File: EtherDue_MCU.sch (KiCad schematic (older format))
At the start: 30 parts, among them SW301 ERASE, SW302 RESET, U301 ATSAM3X8E, U302 FDN340P, U303 LMV358IDGKR, X301 12MHz KX-7 20pF, X302 32.768kHz

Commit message: Final ERC cleanup, export net file
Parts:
- renumbered C301 to C201, C302 to C202, C303 to C203, C304 to C204, C305 to C205, C306 to C206, C307 to C207, C308 to C208, D301 to D201, D302 to D202, D303 to D203, D304 to D204, JR301 to JR201, JR302 to JR202, JR303 to JR203, L301 to L201, R301 to R201, R302 to R202, R303 to R203, R304 to R204, R305 to R205, R306 to R206, SW301 to SW201, SW302 to SW202, U301 to U201, U302 to U202, U303 to U203, X301 to X201, X302 to X202
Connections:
- net +3.3V: now also R206.1 (7), R206.6 (8), R206.8; no longer R206.2 (8), R206.4 (8), R206.5 (7)
- net at D203.A: now also R206.2 (8); no longer R206.6 (8)
- net at U203.1, U203.2 (-): now also R206.3 (7); no longer R206.7
- net at D204.A: now also R206.4 (8); no longer R206.8
- net at D202.A: now also R206.7; no longer R206.3 (7)
- net at D201.A: now also R206.5 (7); no longer R206.1 (7)
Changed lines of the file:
@@
-EESchema Schematic File Version 2  date Thu 11 Apr 2013 15:52:58 EST
+EESchema Schematic File Version 2  date Thu 11 Apr 2013 16:32:55 EST
 LIBS:power
 LIBS:device
@@
 JTAG
 $Comp
-L ATSAM3X8E U301
+L ATSAM3X8E U201
 U 1 1 515B964D
 P 7900 5650
-F 0 "U301" H 5900 3050 50  0000 C CNN
+F 0 "U201" H 5900 3050 50  0000 C CNN
 F 1 "ATSAM3X8E" H 6050 2950 50  0000 C CNN
 F 2 "MODULE" H 6500 3550 50  0001 C CNN
@@
 $EndComp
 $Comp
-L RES_PACK4_IND R305
+L RES_PACK4_IND R205
 U 2 1 5163C001
 P 7300 10150
-F 0 "R305" H 7000 10200 50  0000 C CNN
+F 0 "R205" H 7000 10200 50  0000 C CNN
 F 1 "1K5" H 7300 10050 50  0000 C CNN
 F 2 "" H 7300 10150 60  0001 C CNN
@@
 $EndComp
 $Comp
-L RES_PACK4_IND R305
+L RES_PACK4_IND R205
 U 1 1 5163BFF9
 P 6900 10150
-F 0 "R305" H 6600 10200 50  0000 C CNN
+F 0 "R205" H 6600 10200 50  0000 C CNN
 F 1 "1K5" H 6900 10050 50  0000 C CNN
 F 2 "" H 6900 10150 60  0001 C CNN
@@
 $EndComp
 $Comp
-L R JR301
+L R JR201
 U 1 1 5163BF82
 P 5250 3200
-F 0 "JR301" V 5350 3200 50  0000 C CNN
+F 0 "JR201" V 5350 3200 50  0000 C CNN
 F 1 "0R / NOT PLACED" V 5150 3200 50  0000 C CNN
 F 2 "" H 5250 3200 60  0001 C CNN
@@
 $EndComp
 $Comp
-L R JR303
+L R JR203
 U 1 1 5163BF2B
 P 5800 1150
-F 0 "JR303" V 5880 1150 50  0000 C CNN
+F 0 "JR203" V 5880 1150 50  0000 C CNN
 F 1 "0R NOT PLACED" V 5700 1150 50  0000 C CNN
 F 2 "" H 5800 1150 60  0001 C CNN
@@
 VDDOUT
 $Comp
-L SW_PUSHBUTTON SW302
+L SW_PUSHBUTTON SW202
 U 1 1 515CF2B2
 P 13000 2550
-F 0 "SW302" H 12850 2660 50  0000 C CNN
+F 0 "SW202" H 12850 2660 50  0000 C CNN
 F 1 "RESET" H 13000 2470 50  0000 C CNN
 F 2 "" H 13000 2550 60  0001 C CNN
@@
 $EndComp
 $Comp
-L C C308
+L C C208
 U 1 1 515CF2B0
 P 13000 1950
-F 0 "C308" H 13050 2050 50  0000 L CNN
+F 0 "C208" H 13050 2050 50  0000 L CNN
 F 1 "10nF" H 13050 1850 50  0000 L CNN
 F 2 "" H 13000 1950 60  0001 C CNN
@@
 ERASE
 $Comp
-L MOSFET-PCHANNEL U302
+L MOSFET-PCHANNEL U202
 U 1 1 515CF01A
 P 12000 8950
-F 0 "U302" V 11700 8700 70  0000 L BNN
+F 0 "U202" V 11700 8700 70  0000 L BNN
 F 1 "FDN340P" V 11800 8400 70  0000 L BNN
 F 2 "" H 12000 8950 60  0001 C CNN
@@
 $EndComp
 $Comp
-L SW_PUSHBUTTON SW301
+L SW_PUSHBUTTON SW201
 U 1 1 515CF006
 P 12100 8400
-F 0 "SW301" H 11950 8510 50  0000 C CNN
+F 0 "SW201" H 11950 8510 50  0000 C CNN
 F 1 "ERASE" H 12100 8320 50  0000 C CNN
 F 2 "" H 12100 8400 60  0001 C CNN
@@
 PWM13
 $Comp
-L RES_PACK4_IND R306
-U 1 1 515CBE59
+L RES_PACK4_IND R206
+U 3 1 515CBE59
 P 14450 6500
-F 0 "R306" H 14150 6550 50  0000 C CNN
+F 0 "R206" H 14150 6550 50  0000 C CNN
 F 1 "1K" H 14450 6400 50  0000 C CNN
 F 2 "" H 14450 6500 60  0001 C CNN
 F 3 "" H 14450 6500 60  0001 C CNN
-	1    14450 6500
-	1    0    0    -1
-$EndComp
-$Comp
-L RES_PACK4_IND R306
-U 2 1 515CBE58
+	3    14450 6500
+	1    0    0    -1
+$EndComp
+$Comp
+L RES_PACK4_IND R206
+U 4 1 515CBE58
 P 14450 6800
-F 0 "R306" H 14150 6850 50  0000 C CNN
+F 0 "R206" H 14150 6850 50  0000 C CNN
 F 1 "1K" H 14450 6700 50  0000 C CNN
 F 2 "" H 14450 6800 60  0001 C CNN
 F 3 "" H 14450 6800 60  0001 C CNN
-	2    14450 6800
+	4    14450 6800
 	1    0    0    -1
 $EndComp
@@
 $EndComp
 $Comp
-L LED D301
+L LED D201
 U 1 1 515CBE56
 P 13800 6500
-F 0 "D301" H 13800 6600 50  0000 C CNN
+F 0 "D201" H 13800 6600 50  0000 C CNN
 F 1 "YELLOW" H 13800 6400 50  0000 C CNN
 F 2 "" H 13800 6500 60  0001 C CNN
@@
 $EndComp
 $Comp
-L LED D302
+L LED D202
 U 1 1 515CBE55
 P 13800 6800
-F 0 "D302" H 13800 6900 50  0000 C CNN
+F 0 "D202" H 13800 6900 50  0000 C CNN
 F 1 "YELLOW" H 13800 6700 50  0000 C CNN
 F 2 "" H 13800 6800 60  0001 C CNN
@@
 $EndComp
 $Comp
-L LED D304
+L LED D204
 U 1 1 515CBD0A
 P 14950 5500
-F 0 "D304" H 14950 5600 50  0000 C CNN
+F 0 "D204" H 14950 5600 50  0000 C CNN
 F 1 "YELLOW" H 14950 5400 50  0000 C CNN
 F 2 "" H 14950 5500 60  0001 C CNN
@@
 $EndComp
 $Comp
-L LED D303
+L LED D203
 U 1 1 515CBD09
 P 14950 5150
-F 0 "D303" H 14950 5250 50  0000 C CNN
+F 0 "D203" H 14950 5250 50  0000 C CNN
 F 1 "GREEN" H 14950 5050 50  0000 C CNN
 F 2 "" H 14950 5150 60  0001 C CNN
@@
 $EndComp
 $Comp
-L LM358 U303
+L LM358 U203
 U 1 1 515CBD06
 P 13250 5500
-F 0 "U303" H 13200 5700 60  0000 L CNN
+F 0 "U203" H 13200 5700 60  0000 L CNN
 F 1 "LMV358IDGKR" H 13200 5250 60  0000 L CNN
 F 2 "" H 13250 5500 60  0001 C CNN
@@
 $Comp
 L RES_PACK4_IND R206
-U 4 1 515CBD03
+U 2 1 515CBD03
 P 14150 5500
 F 0 "R206" H 13850 5550 50  0000 C CNN
@@
 F 2 "" H 14150 5500 60  0001 C CNN
 F 3 "" H 14150 5500 60  0001 C CNN
-	4    14150 5500
+	2    14150 5500
 	1    0    0    -1
 $EndComp
@@
 $Comp
 L RES_PACK4_IND R206
-U 3 1 515CBD02
+U 1 1 515CBD02
 P 14150 5150
 F 0 "R206" H 13850 5200 50  0000 C CNN
@@
 F 2 "" H 14150 5150 60  0001 C CNN
 F 3 "" H 14150 5150 60  0001 C CNN
-	3    14150 5150
+	1    14150 5150
 	1    0    0    -1
 $EndComp
@@
 $EndComp
 $Comp
-L R R301
+L R R201
 U 1 1 515BAA3A
 P 3400 5500
-F 0 "R301" V 3480 5500 50  0000 C CNN
+F 0 "R201" V 3480 5500 50  0000 C CNN
 F 1 "6k8 1%" V 3400 5500 50  0000 C CNN
 F 2 "" H 3400 5500 60  0001 C CNN
@@
 $EndComp
 $Comp
-L C C305
+L C C205
 U 1 1 515BAA2B
 P 3800 5500
-F 0 "C305" H 3850 5600 50  0000 L CNN
+F 0 "C205" H 3850 5600 50  0000 L CNN
 F 1 "22pF" H 3850 5400 50  0000 L CNN
 F 2 "" H 3800 5500 60  0001 C CNN
@@
 $EndComp
 $Comp
-L R R302
+L R R202
 U 1 1 515BA9DE
 P 5200 4100
-F 0 "R302" V 5280 4100 50  0000 C CNN
+F 0 "R202" V 5280 4100 50  0000 C CNN
 F 1 "39R 1%" V 5200 4100 50  0000 C CNN
 F 2 "" H 5200 4100 60  0001 C CNN
@@
 $EndComp
 $Comp
-L R R303
+L R R203
 U 1 1 515BA9D0
 P 5200 4300
-F 0 "R303" V 5280 4300 50  0000 C CNN
+F 0 "R203" V 5280 4300 50  0000 C CNN
 F 1 "39R 1%" V 5200 4300 50  0000 C CNN
 F 2 "" H 5200 4300 60  0001 C CNN
@@
 $EndComp
 $Comp
-L C C304
+L C C204
 U 1 1 515BA7F4
 P 3200 4900
-F 0 "C304" H 3250 5000 50  0000 L CNN
+F 0 "C204" H 3250 5000 50  0000 L CNN
 F 1 "22pF_NM" V 3300 4500 50  0000 L CNN
 F 2 "" H 3200 4900 60  0001 C CNN
@@
 $EndComp
 $Comp
-L C C303
+L C C203
 U 1 1 515BA7D3
 P 3200 4150
-F 0 "C303" H 3250 4250 50  0000 L CNN
+F 0 "C203" H 3250 4250 50  0000 L CNN
 F 1 "22pF_NM" V 3300 3750 50  0000 L CNN
 F 2 "" H 3200 4150 60  0001 C CNN
@@
 $EndComp
 $Comp
-L CRYSTAL X302
+L CRYSTAL X202
 U 1 1 515BA7AB
 P 3750 4450
-F 0 "X302" H 3750 4600 60  0000 C CNN
+F 0 "X202" H 3750 4600 60  0000 C CNN
 F 1 "32.768kHz" H 3750 4300 60  0000 C CNN
 F 2 "" H 3750 4450 60  0001 C CNN
@@
 $EndComp
 $Comp
-L C C302
+L C C202
 U 1 1 515BA78E
 P 3200 3750
-F 0 "C302" H 3250 3850 50  0000 L CNN
+F 0 "C202" H 3250 3850 50  0000 L CNN
 F 1 "22pF" H 3250 3650 50  0000 L CNN
 F 2 "" H 3200 3750 60  0001 C CNN
@@
 $EndComp
 $Comp
-L C C301
+L C C201
 U 1 1 515BA78B
 P 3200 2700
-F 0 "C301" H 3250 2800 50  0000 L CNN
+F 0 "C201" H 3250 2800 50  0000 L CNN
 F 1 "22pF" H 3250 2600 50  0000 L CNN
 F 2 "" H 3200 2700 60  0001 C CNN
@@
 $EndComp
 $Comp
-L CRYSTAL X301
+L CRYSTAL X201
 U 1 1 515BA76A
 P 3750 3150
-F 0 "X301" H 3750 3300 60  0000 C CNN
+F 0 "X201" H 3750 3300 60  0000 C CNN
 F 1 "12MHz KX-7 20pF" H 3800 3000 60  0000 C CNN
 F 2 "" H 3750 3150 60  0001 C CNN
@@
 $EndComp
 $Comp
-L R JR302
+L R JR202
 U 1 1 515BA19D
 P 5800 950
-F 0 "JR302" V 5880 950 50  0000 C CNN
+F 0 "JR202" V 5880 950 50  0000 C CNN
 F 1 "0R" V 5800 950 50  0000 C CNN
 F 2 "" H 5800 950 60  0001 C CNN
@@
 $EndComp
 $Comp
-L C C306
+L C C206
 U 1 1 515B9982
 P 6300 1450
-F 0 "C306" H 6350 1550 50  0000 L CNN
+F 0 "C206" H 6350 1550 50  0000 L CNN
 F 1 "100nF" H 6350 1350 50  0000 L CNN
 F 2 "" H 6300 1450 60  0001 C CNN
@@
 $EndComp
 $Comp
-L C C307
+L C C207
 U 1 1 515B9979
 P 7150 1350
-F 0 "C307" H 7050 1450 50  0000 L CNN
+F 0 "C207" H 7050 1450 50  0000 L CNN
 F 1 "100nF" H 6900 1250 50  0000 L CNN
 F 2 "" H 7150 1350 60  0001 C CNN
@@
 $EndComp
 $Comp
-L INDUCTOR L301
+L INDUCTOR L201
 U 1 1 515B996F
 P 6700 1100
-F 0 "L301" V 6650 1100 40  0000 C CNN
+F 0 "L201" V 6650 1100 40  0000 C CNN
 F 1 "MH2029-300Y" V 6800 1100 40  0000 C CNN
 F 2 "" H 6700 1100 60  0001 C CNN
@@
 $EndComp
 $Comp
-L R R304
+L R R204
 U 1 1 515B98E9
 P 6750 2300
-F 0 "R304" V 6830 2300 50  0000 C CNN
+F 0 "R204" V 6830 2300 50  0000 C CNN
 F 1 "100K" V 6750 2300 50  0000 C CNN
 F 2 "" H 6750 2300 60  0001 C CNN

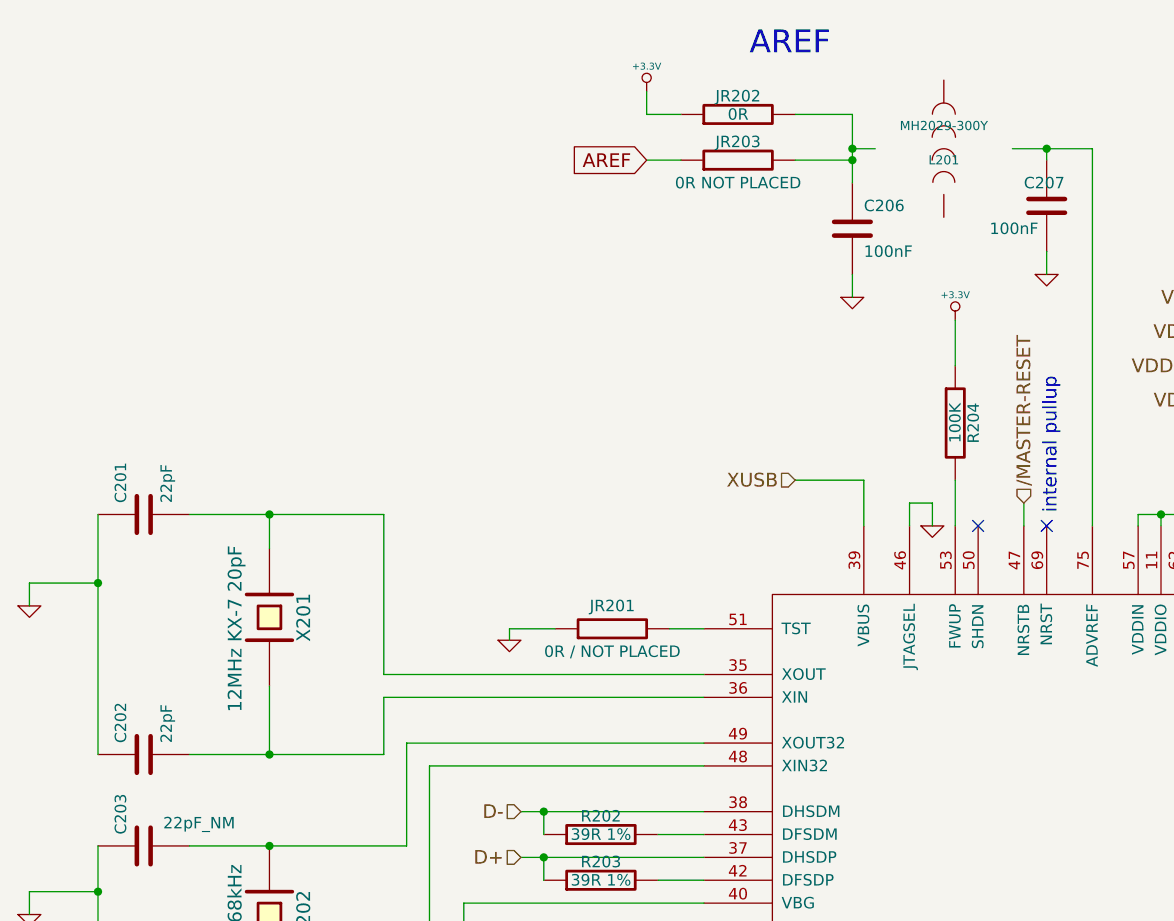
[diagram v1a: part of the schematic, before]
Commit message: Edit pass of footprints, cleanup symbols, etc.
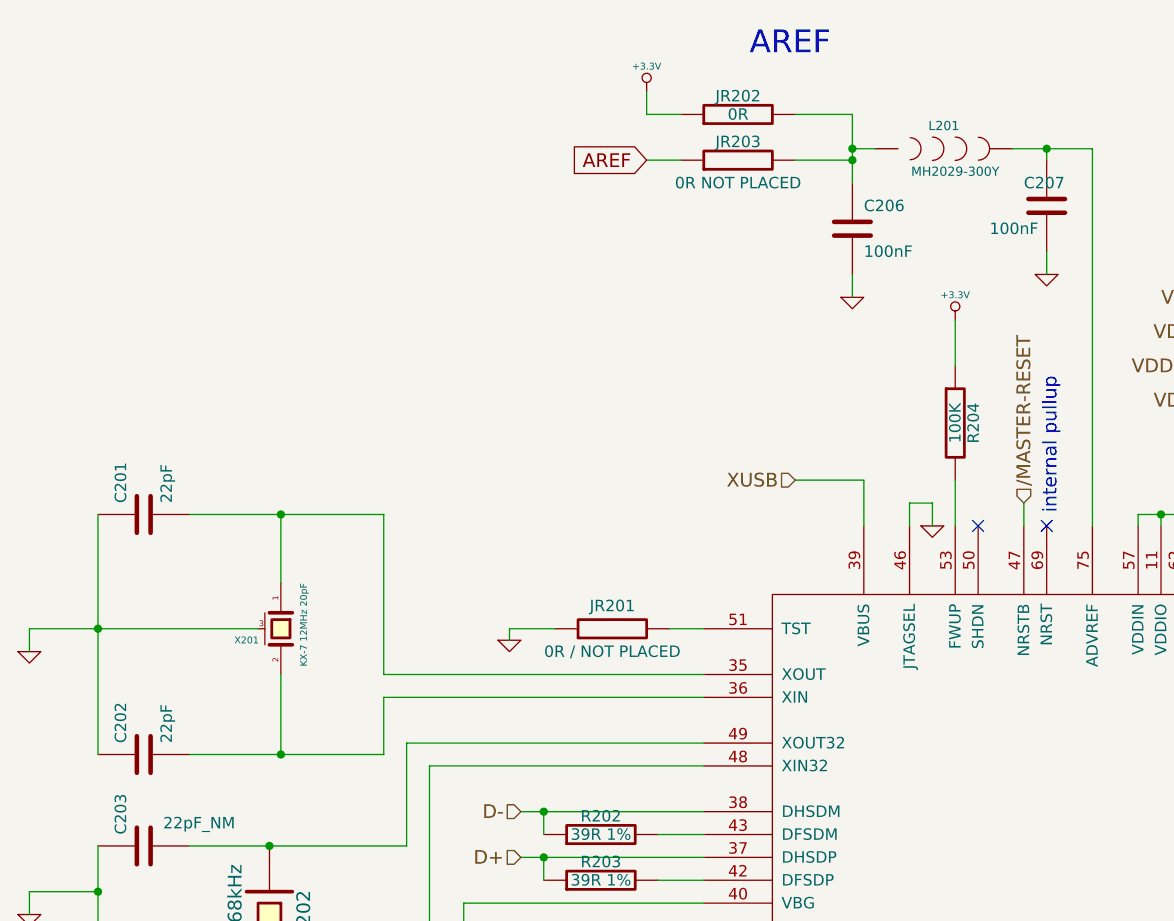
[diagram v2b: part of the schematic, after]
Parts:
- removed X201: 12MHz KX-7 20pF, symbol CRYSTAL
- added X201: KX-7 12MHz 20pF, ~, symbol CRYSTAL_SMD
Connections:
- net GND: now also X201.3 (case)
- net at C201.2, U201.35 (XOUT): now also X201.1
- net at C202.2, U201.36 (XIN): now also X201.2
- net at C207.1, U201.75 (ADVREF): now also L201.2
- net at L201.1: now also C206.1, JR202.2, JR203.2
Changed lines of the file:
@@
-EESchema Schematic File Version 2  date Thu 11 Apr 2013 16:32:55 EST
+EESchema Schematic File Version 2  date Fri 03 May 2013 15:34:29 EST
+LIBS:freetronics_kicad_sch_lib
 LIBS:power
 LIBS:device
@@
 LIBS:contrib
 LIBS:valves
-LIBS:freetronics_kicad_sch_lib
 LIBS:EtherDue-cache
 EELAYER 24 0
@@
 Sheet 2 6
 Title ""
-Date "11 apr 2013"
+Date "3 may 2013"
 Rev ""
 Comp ""
@@
 Wire Wire Line
 	2700 4350 2700 4450
-Connection ~ 3750 3750
 Wire Wire Line
 	5650 3500 4250 3500
@@
 Wire Wire Line
 	4250 3750 3400 3750
-Connection ~ 3000 3000
+Connection ~ 3000 3200
 Wire Wire Line
 	3000 3750 3000 2700
-Connection ~ 3750 2700
 Wire Wire Line
 	3400 2700 4250 2700
@@
 Wire Wire Line
 	4250 3400 5650 3400
-Wire Wire Line
-	3750 2700 3750 2850
-Wire Wire Line
-	3000 3000 2700 3000
-Wire Wire Line
-	2700 3000 2700 3100
-Wire Wire Line
-	3750 3750 3750 3450
 Wire Wire Line
 	3000 4150 3000 4900
@@
 L GND #PWR010
 U 1 1 515BA7A2
-P 2700 3100
-F 0 "#PWR010" H 2700 3100 30  0001 C CNN
-F 1 "GND" H 2700 3030 30  0001 C CNN
-F 2 "" H 2700 3100 60  0001 C CNN
-F 3 "" H 2700 3100 60  0001 C CNN
-	1    2700 3100
+P 2700 3300
+F 0 "#PWR010" H 2700 3300 30  0001 C CNN
+F 1 "GND" H 2700 3230 30  0001 C CNN
+F 2 "" H 2700 3300 60  0001 C CNN
+F 3 "" H 2700 3300 60  0001 C CNN
+	1    2700 3300
 	1    0    0    -1
 $EndComp
@@
 	1    3200 2700
 	0    -1   -1   0
-$EndComp
-$Comp
-L CRYSTAL X201
-U 1 1 515BA76A
-P 3750 3150
-F 0 "X201" H 3750 3300 60  0000 C CNN
-F 1 "12MHz KX-7 20pF" H 3800 3000 60  0000 C CNN
-F 2 "" H 3750 3150 60  0001 C CNN
-F 3 "" H 3750 3150 60  0001 C CNN
-	1    3750 3150
-	0    1    1    0
 $EndComp
 $Comp
@@
 U 1 1 515B996F
 P 6700 1100
-F 0 "L201" V 6650 1100 40  0000 C CNN
-F 1 "MH2029-300Y" V 6800 1100 40  0000 C CNN
+F 0 "L201" H 6700 1200 40  0000 C CNN
+F 1 "MH2029-300Y" H 6750 1000 40  0000 C CNN
 F 2 "" H 6700 1100 60  0001 C CNN
 F 3 "" H 6700 1100 60  0001 C CNN
 	1    6700 1100
-	0    -1   -1   0
+	1    0    0    -1
 $EndComp
 Text Notes 7200 2700 1    60   ~ 0
@@
 	1    0    0    -1
 $EndComp
+$Comp
+L CRYSTAL_SMD X201
+U 1 1 516FA5C5
+P 3800 3200
+F 0 "X201" V 3850 3050 30  0000 C CNN
+F 1 "KX-7 12MHz  20pF" H 3600 3300 30  0000 L CNN
+F 2 "~" H 3800 3200 60  0000 C CNN
+F 3 "~" H 3800 3200 60  0000 C CNN
+	1    3800 3200
+	0    1    1    0
+$EndComp
+Wire Wire Line
+	2700 3200 3700 3200
+Wire Wire Line
+	3800 3000 3800 2700
+Connection ~ 3800 2700
+Wire Wire Line
+	3800 3400 3800 3750
+Connection ~ 3800 3750
+Wire Wire Line
+	2700 3200 2700 3300
 $EndSCHEMATC

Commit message: General clean up, component selection, etc.
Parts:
- renumbered U201 to IC201
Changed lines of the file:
@@
-EESchema Schematic File Version 2  date Fri 03 May 2013 15:34:29 EST
+EESchema Schematic File Version 2  date Tue 04 Jun 2013 15:53:49 EST
 LIBS:freetronics_kicad_sch_lib
 LIBS:power
@@
 Sheet 2 6
 Title ""
-Date "3 may 2013"
+Date "4 jun 2013"
 Rev ""
 Comp ""
@@
 JTAG
 $Comp
-L ATSAM3X8E U201
+L ATSAM3X8E IC201
 U 1 1 515B964D
 P 7900 5650
-F 0 "U201" H 5900 3050 50  0000 C CNN
+F 0 "IC201" H 5900 3050 50  0000 C CNN
 F 1 "ATSAM3X8E" H 6050 2950 50  0000 C CNN
 F 2 "MODULE" H 6500 3550 50  0001 C CNN
